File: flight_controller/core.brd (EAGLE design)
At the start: 102 x 82 mm, 115 parts, among them J1 M02, J10 M02, J11 M02, J12 M02, J13 M02, J14 M02, J15 M02, J16 M03, J17 M03, J18 M04, J19 M04, J2 M02, J20 M03, J21 M04, J3 M02, J4 M03, J5 M02, J6 M02, J7 M02, J8 M02, J9 M03, Q1 EM6K1, Q2 EM6K1, Q3 EM6K1, Q4 EM6K1, Q5 EM6K1, Q6 EM6K1, Q7 MOSFET-PCHANNEL-AON6407, U1 STM32F405, U2 MEAS-MS5611, U3 MPU-9250-QFN-24-NP, U4 MIC5219 3.3V, U5 USD-SOCKETNEW, Y1 16MHz

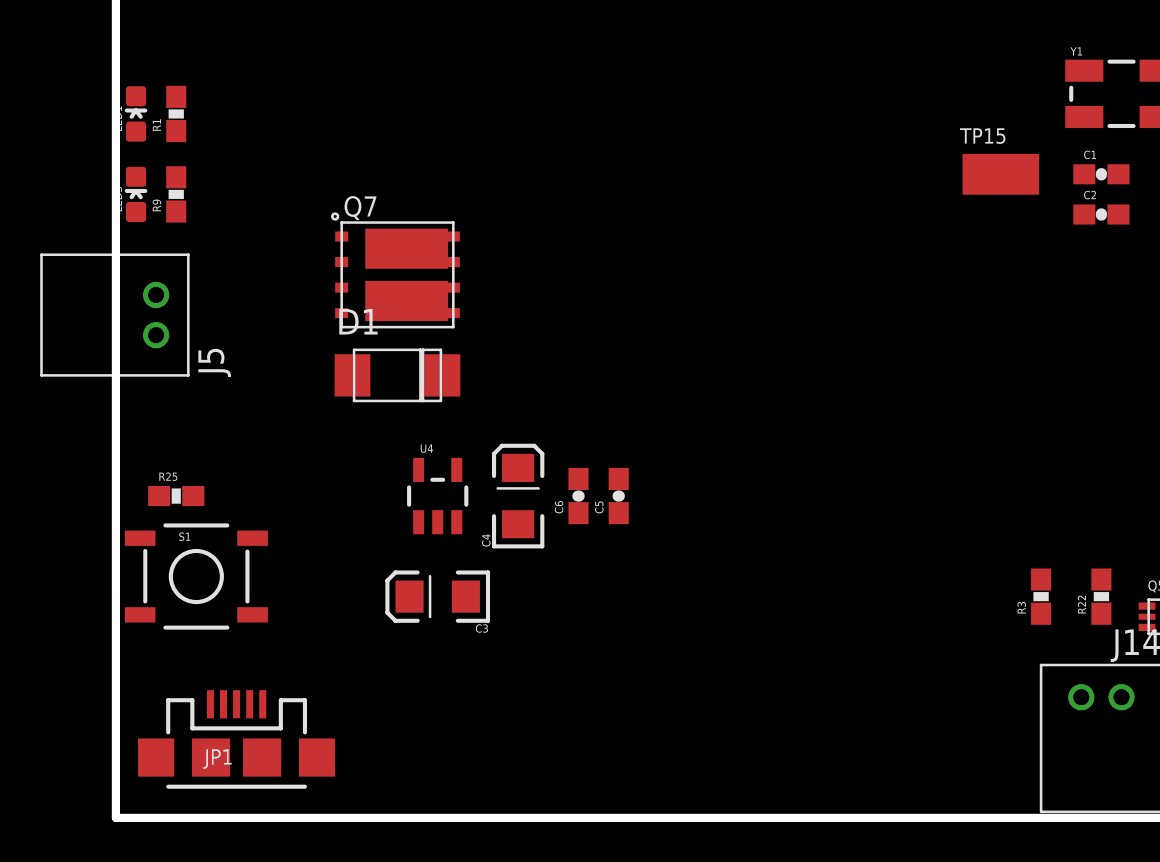
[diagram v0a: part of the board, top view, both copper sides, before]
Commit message: Move USB 5V to VIN.
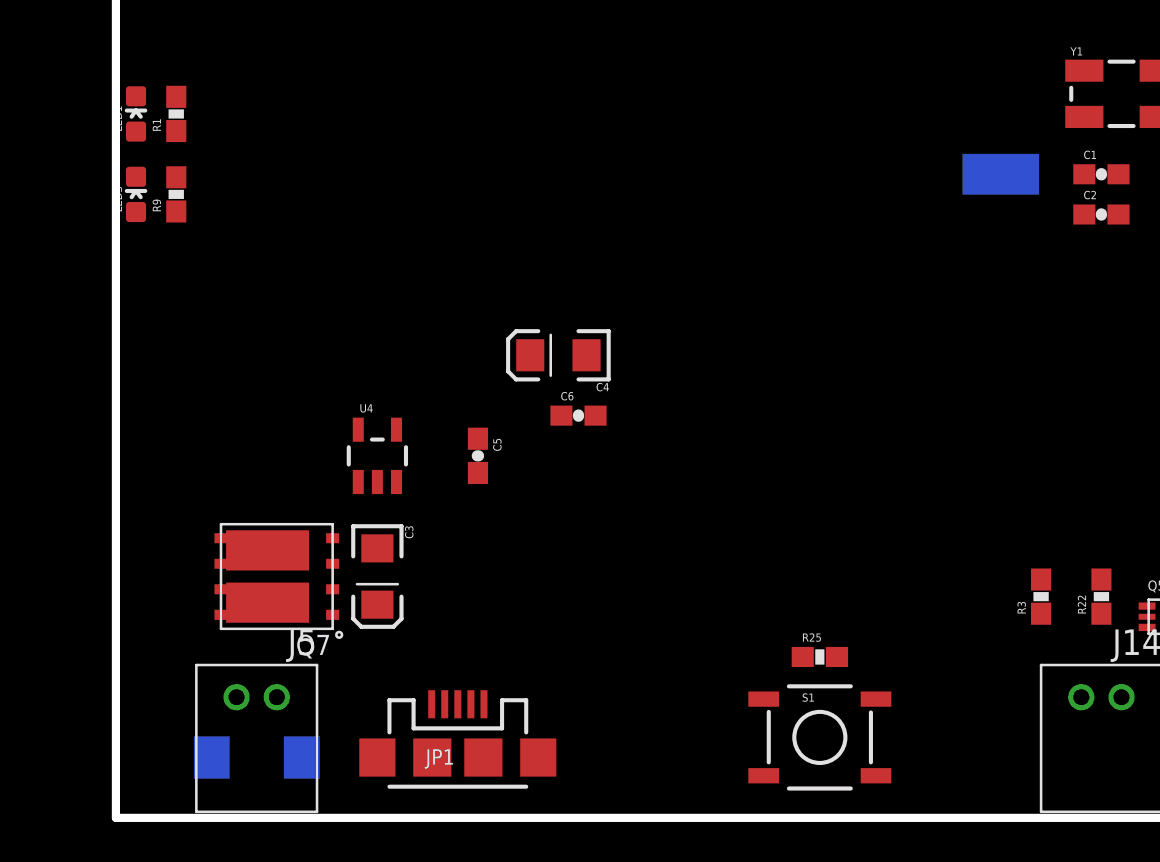
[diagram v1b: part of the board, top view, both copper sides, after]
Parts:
- moved R25 33.0 mm to (35.0, 8.00)
- moved S1 32.0 mm to (35.0, 4.00)
- moved D1 20.2 mm to (7.00, 3.00), flipped to the bottom, turned to 180 degrees
- moved J5 19.0 mm to (8.00, 6.00), turned to 180 degrees
- moved Q7 16.2 mm to (8.00, 12.0), turned to 180 degrees
- moved JP1 11.0 mm to (17.0, 3.00)
- moved C4 7.28 mm to (22.0, 23.0), turned to 180 degrees
- moved C5 7.28 mm to (18.0, 18.0), turned to 270 degrees
- moved C6 4.00 mm to (23.0, 20.0), turned to 0 degrees
- moved U4 3.61 mm to (13.0, 18.0)
- moved C3 3.16 mm to (13.0, 12.0), turned to 270 degrees
- flipped TP15 to the bottom
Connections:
- net 5V: no longer JP1.VBUS
- net VIN: now also JP1.VBUS

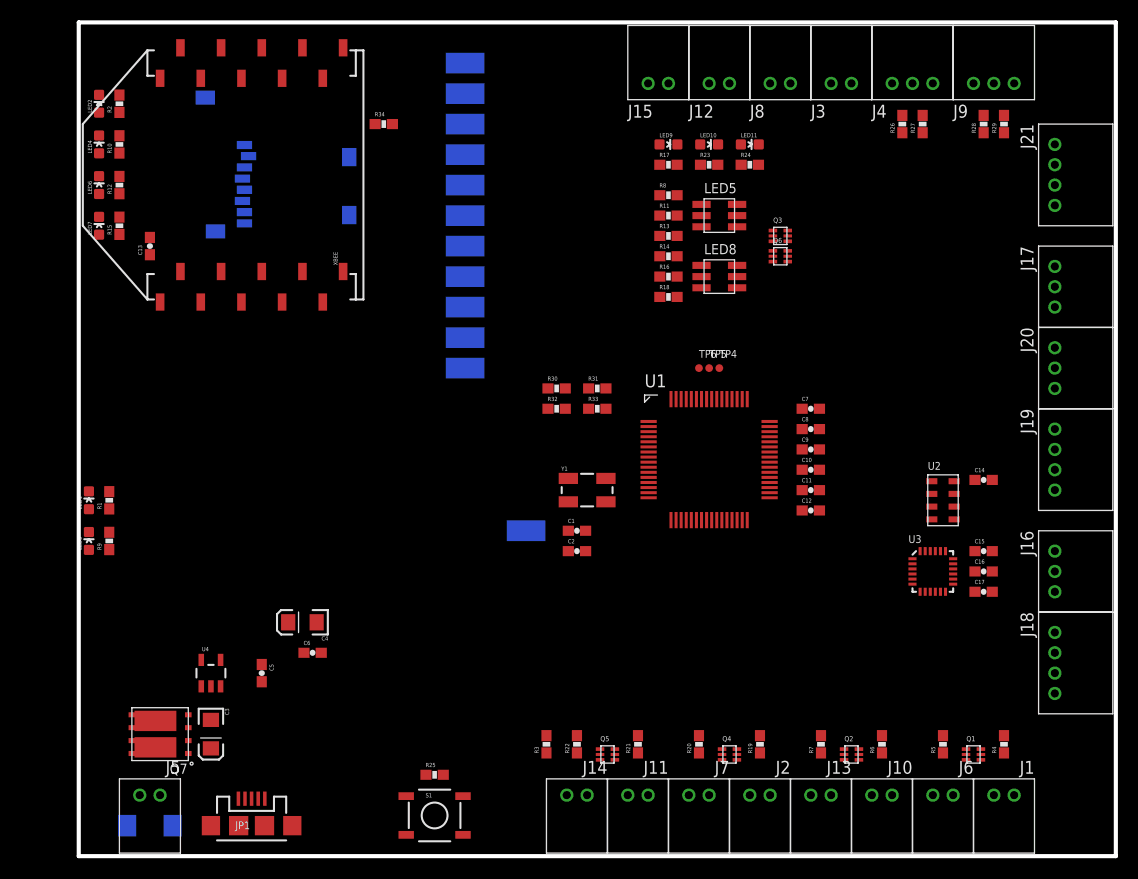
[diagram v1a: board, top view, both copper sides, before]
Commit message: Make last two PWM outputs 5V powered (for servos).
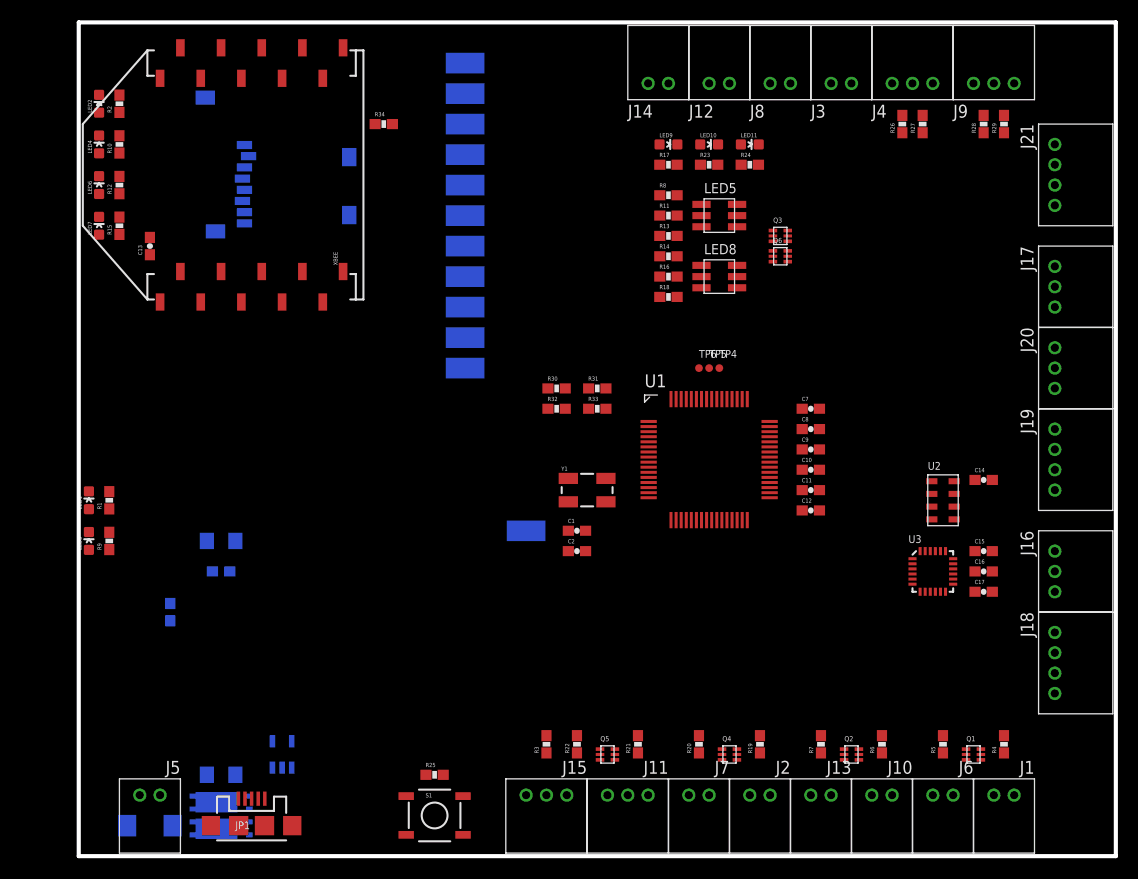
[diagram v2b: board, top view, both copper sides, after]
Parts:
- J11, J15: value M02 -> M03; device OSURC_Connectors:MOLEX-2MM-MICROLATCH-2POS-RA -> OSURC_Connectors:MOLEX-2MM-MICROLATCH-3POS-RA
- moved J15 70.5 mm to (48.0, 6.00), turned to 180 degrees
- moved J14 70.3 mm to (56.0, 76.0), turned to 0 degrees
- moved C6 12.0 mm to (14.0, 28.0), flipped to the bottom
- moved C4 11.3 mm to (14.0, 31.0), flipped to the bottom
- moved C5 10.8 mm to (9.00, 24.0), flipped to the bottom
- moved U4 10.6 mm to (20.0, 10.0), flipped to the bottom
- moved Q7 10.0 mm to (14.0, 4.00), flipped to the bottom, turned to 0 degrees
- moved C3 4.12 mm to (14.0, 8.00), flipped to the bottom, turned to 180 degrees
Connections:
- net 5V: now also J11.2, J15.2
- net GND: now also J11.3, J15.3; no longer J11.2, J15.2
- net PC5: now also J14.1; no longer J15.1
- net TIM4-CH4-K: now also J15.1; no longer J14.1

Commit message: Component placement almost done, routing halfway done.
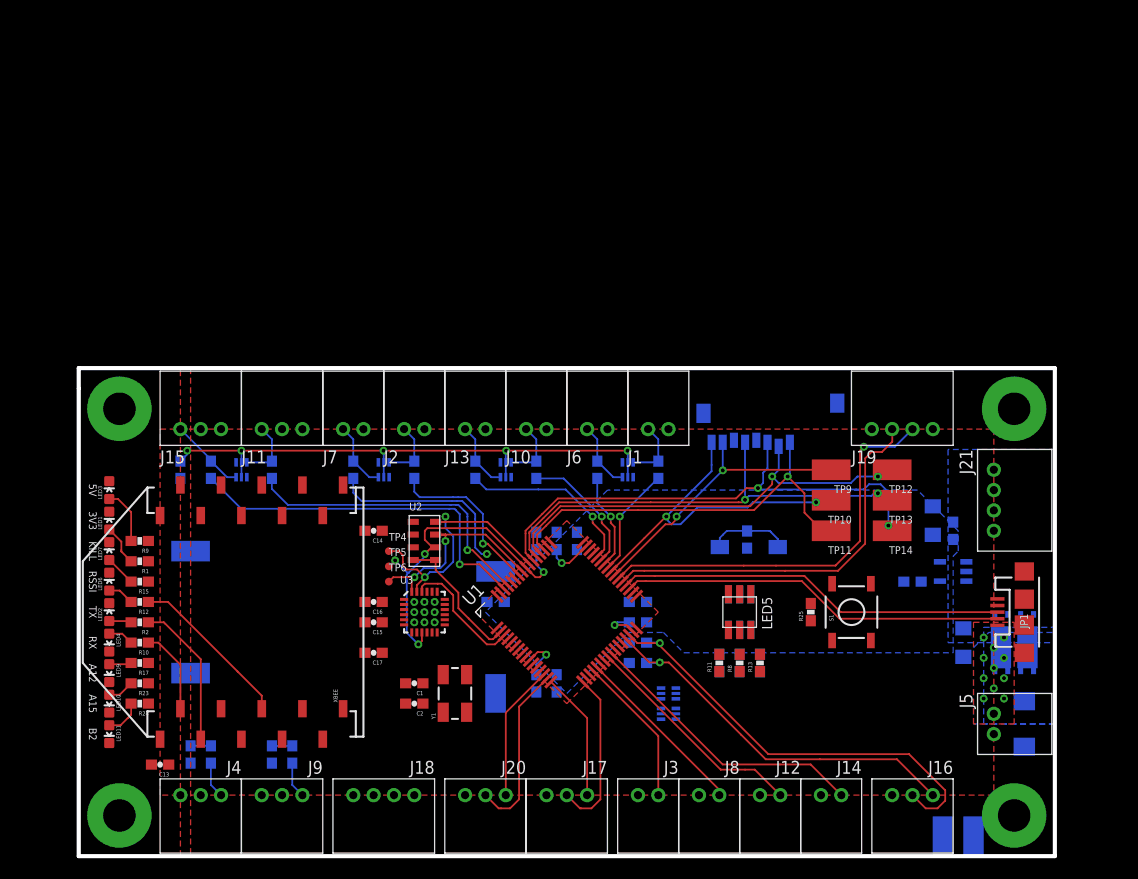
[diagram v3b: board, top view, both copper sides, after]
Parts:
- added S2, S3, S4, S5: STANDOFF_ELECTRICAL-#4, OSURC_Electromechanical:STANDOFF-ELECTRICAL-#4
- moved J4 96.2 mm to (14.0, 6.00), turned to 180 degrees
- moved J9 96.2 mm to (22.0, 6.00), turned to 180 degrees
- moved R27 95.0 mm to (11.0, 10.0), flipped to the bottom, turned to 270 degrees
- moved R29 95.0 mm to (19.0, 10.0), flipped to the bottom, turned to 270 degrees
- moved R26 92.0 mm to (13.0, 10.0), flipped to the bottom, turned to 270 degrees
- moved R28 92.0 mm to (21.0, 10.0), flipped to the bottom, turned to 270 degrees
- moved D1 86.6 mm to (93.0, 13.0), turned to 90 degrees
- moved LED11 85.6 mm to (3.00, 12.0), turned to 180 degrees
- moved TP7 83.6 mm to (88.0, 2.00), turned to 270 degrees
- moved J5 82.4 mm to (90.0, 14.0), turned to 270 degrees
- moved LED10 80.7 mm to (3.00, 15.0), turned to 180 degrees
- moved R24 80.1 mm to (6.00, 15.0), turned to 180 degrees
- moved Q7 79.8 mm to (92.0, 21.0), turned to 270 degrees
- moved TP8 79.4 mm to (85.0, 2.00), turned to 270 degrees
- moved JP1 78.8 mm to (93.0, 24.0), turned to 90 degrees
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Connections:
- net N$12 renamed STSB1+
- net N$15 renamed STSR2+
- net N$16 renamed STSG2+
- net N$19 renamed STSB2+
- net N$5 renamed STSB-
- net N$6 renamed STSG-
- net N$7 renamed STSR-
- net N$8 renamed STSR1+
- net N$9 renamed STSG1+
- removed net OTG-HS-ID: U1.33
- net GND: now also S2.P1, S3.P1, S4.P1, S5.P1
- net USD-CD: now also U1.33
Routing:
- net KILL: track 0.00 -> 55.1 mm, vias 0 -> 5
- net SDIO-CMD: track 0.00 -> 50.1 mm, vias 0 -> 2
- net SDIO-CK: track 0.00 -> 45.9 mm, vias 0 -> 2
- net SDIO-D3: track 0.00 -> 44.3 mm, vias 0 -> 2
- net I2C2-SDA: track 0.00 -> 44.0 mm, vias 0 -> 1
- net UART6-RX-GPS: track 0.00 -> 40.2 mm, vias 0 -> 1
- net SDIO-D2: track 0.00 -> 39.8 mm, vias 0 -> 1
- net UART6-TX-GPS: track 0.00 -> 38.4 mm
- net OTG-HS-DP: track 0.00 -> 38.4 mm
- net OTG-HS-DM: track 0.00 -> 38.1 mm
- net I2C2-SCL: track 0.00 -> 37.9 mm, vias 0 -> 1
- net TIM4-CH4: track 0.00 -> 36.3 mm, vias 0 -> 1
- net SDIO-D1: track 0.00 -> 34.4 mm, vias 0 -> 2
- net SPI1-MISO: track 0.00 -> 34.0 mm, vias 0 -> 4
- net TIM4-CH3: track 0.00 -> 30.3 mm, vias 0 -> 1
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- added copper zone on layer 1, net 3.3V
- added copper zone on layer 16, net 3.3V
- added copper zone on layer 1, net 5V
- added copper zone on layer 16, net 5V
- added copper zone on layer 1, net GND
- added copper zone on layer 16, net GND
- added copper zone on layer 1, net VIN
- added copper zone on layer 16, net VIN
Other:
- board size 102 x 82 mm -> 96 x 48 mm
- board text added: "3V3"
- board text added: "5V"
- board text added: "A12"
- board text added: "A15"
- board text added: "B2"
- board text added: "KILL"
- board text added: "RSSI"
- board text added: "RX"
- board text added: "TX"

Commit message: More layout, and replace passives with OSURC's own.
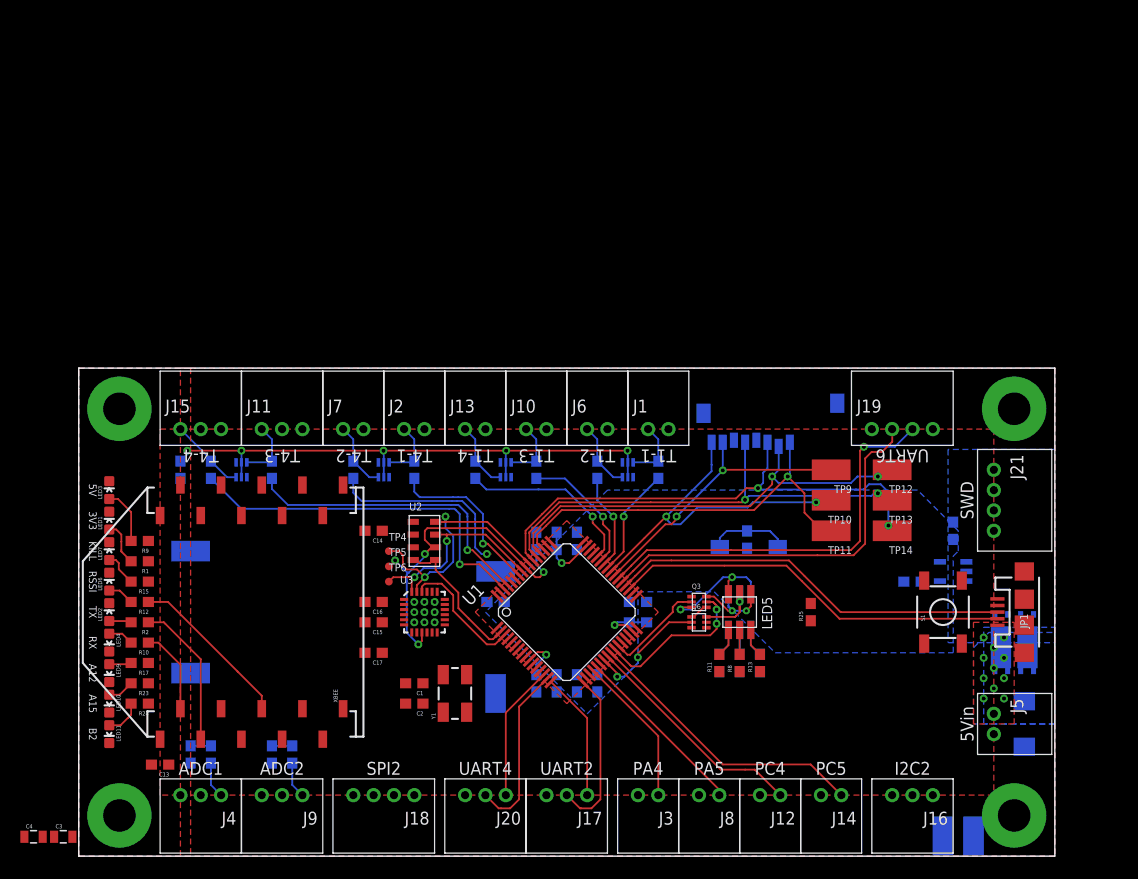
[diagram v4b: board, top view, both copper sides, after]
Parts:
- C1, C11, C12, C16, C2, C5: device SparkFun-Capacitors:0603-CAP -> OSURC_Passives:0603
- C10, C13, C14, C15, C17, C6, C7, C8, C9: value 0.1uF -> 100nF; device SparkFun-Capacitors:0603-CAP -> OSURC_Passives:0603
- C3, C4: device SparkFun-Capacitors:EIA3216 -> OSURC_Passives:0805
- R1, R10, R11, R12, R13, R14, R15, R16, R17, R18, R2, R23, R24, R8: device SparkFun-Passives:0603-RES -> OSURC_Passives:0603
- R19, R20, R21, R22, R3, R4, R5, R6, R7: value 1K -> 1k; device SparkFun:0603-RES -> OSURC_Passives:0603
- R25: value 20K -> 20k; device SparkFun:0603-RES -> OSURC_Passives:0603
- R26, R27, R28, R29, R30, R32: value 20K -> 20k; device SparkFun-Passives:0603-RES -> OSURC_Passives:0603
- R31, R33: value 1K5 -> 1.5k; device SparkFun-Passives:0603-RES -> OSURC_Passives:0603
- R34: value 1K -> 1k; device SparkFun-Passives:0603-RES -> OSURC_Passives:0603
- R9: value 1K1 -> 1.1k; device SparkFun-Passives:0603-RES -> OSURC_Passives:0603
- S1: value SWITCH-MOMENTARY-2SMD -> SWITCH-MOMENTARY-2-PTS525; device SparkFun-Electromechanical:TACTILE-SWITCH-SMD -> OSURC_Electromechanical:TACTILE-SWITCH-SMD
- moved C4 93.8 mm to (-4.45, 1.91), flipped to the top, turned to 0 degrees
- moved C3 90.6 mm to (-1.52, 1.91), flipped to the top, turned to 0 degrees
- moved Q3 9.49 mm to (61.0, 25.0), flipped to the top
- moved Q6 9.49 mm to (61.0, 23.0), flipped to the top, turned to 0 degrees
- moved S1 9.00 mm to (85.0, 24.0)
- moved R33 7.21 mm to (49.0, 17.0), turned to 90 degrees
- moved R31 4.47 mm to (51.0, 17.0), turned to 90 degrees
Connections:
- net 3.3V: now also C10.2, C13.2, C14.2, C15.2, C16.2, C4.2, C6.2, C8.2, C9.2; no longer C10.1, C13.1, C14.1, C15.1, C16.1, C4.A, C6.1, C8.1, C9.1
- net 5V: now also C3.2; no longer C3.A
- net F4-VCAP-1: now also C11.2; no longer C11.1
- net F4-VCAP-2: now also C12.2; no longer C12.1
- net GND: now also C1.1, C10.1, C11.1, C12.1, C13.1, C14.1, C15.1, C16.1, C17.1, C2.1, C3.1, C4.1, C5.1, C6.1, C8.1, C9.1, S1.4; no longer C1.2, C10.2, C11.2, C12.2, C13.2, C14.2, C15.2, C16.2, C17.2, C2.2, C3.C, C4.C, C5.2, C6.2, C8.2, C9.2
- net MIC-BP: now also C5.2; no longer C5.1
- net MPU9250-REGOUT: now also C17.2; no longer C17.1
- net OSC-IN: now also C1.2; no longer C1.1
- net OSC-OUT: now also C2.2; no longer C2.1
- net RST: now also S1.2
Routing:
- net I2C2-SDA: track 44.0 -> 0.00 mm, vias 1 -> 0
- net I2C2-SCL: track 37.9 -> 0.00 mm, vias 1 -> 0
- net TIM3-CH3-STSG: track 0.00 -> 15.7 mm, vias 0 -> 2
- net STSG-: track 0.00 -> 12.7 mm, vias 0 -> 2
- net TIM3-CH2-STSR: track 0.00 -> 12.2 mm, vias 0 -> 2
- net TIM3-CH4-STSB: track 0.00 -> 9.98 mm
- net STSB-: track 0.00 -> 8.08 mm, vias 0 -> 2
- net STSR-: track 0.00 -> 6.85 mm, vias 0 -> 1
- net STSG2+: track 0.00 -> 2.77 mm
- net STSB1+: track 0.00 -> 2.77 mm
- net STSG1+: track 0.00 -> 2.77 mm
- net STSB2+: track 0.00 -> 2.77 mm
- net STSR2+: track 0.00 -> 2.40 mm
- net STSR1+: track 0.00 -> 2.40 mm
- net GND: track 0.00 -> 1.85 mm
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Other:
- board text added: "5Vin"
- board text added: "ADC1"
- board text added: "ADC2"
- board text added: "I2C2"
- board text added: "PA4"
- board text added: "PA5"
- board text added: "PC4"
- board text added: "PC5"
- board text added: "SPI2"
- board text added: "SWD"
- board text added: "T1-1"
- board text added: "T1-2"
- board text added: "T1-3"
- board text added: "T1-4"
- board text added: "T4-1"
- board text added: "T4-2"
- board text added: "T4-3"
- board text added: "T4-4"
- board text added: "UART2"
- board text added: "UART4"
- board text added: "UART6"
